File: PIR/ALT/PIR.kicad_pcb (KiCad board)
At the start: 2 copper layers, 30 x 90 mm, 29 parts, among them J1 BUS, J2 BATT_EXT, J5 FLASH/CONF, J6 PIR, Q1 BC846, Q2 BC846, Q3 BC857, SW1 tamper switch, U1 AP63203WU, U2 WT8266-S1

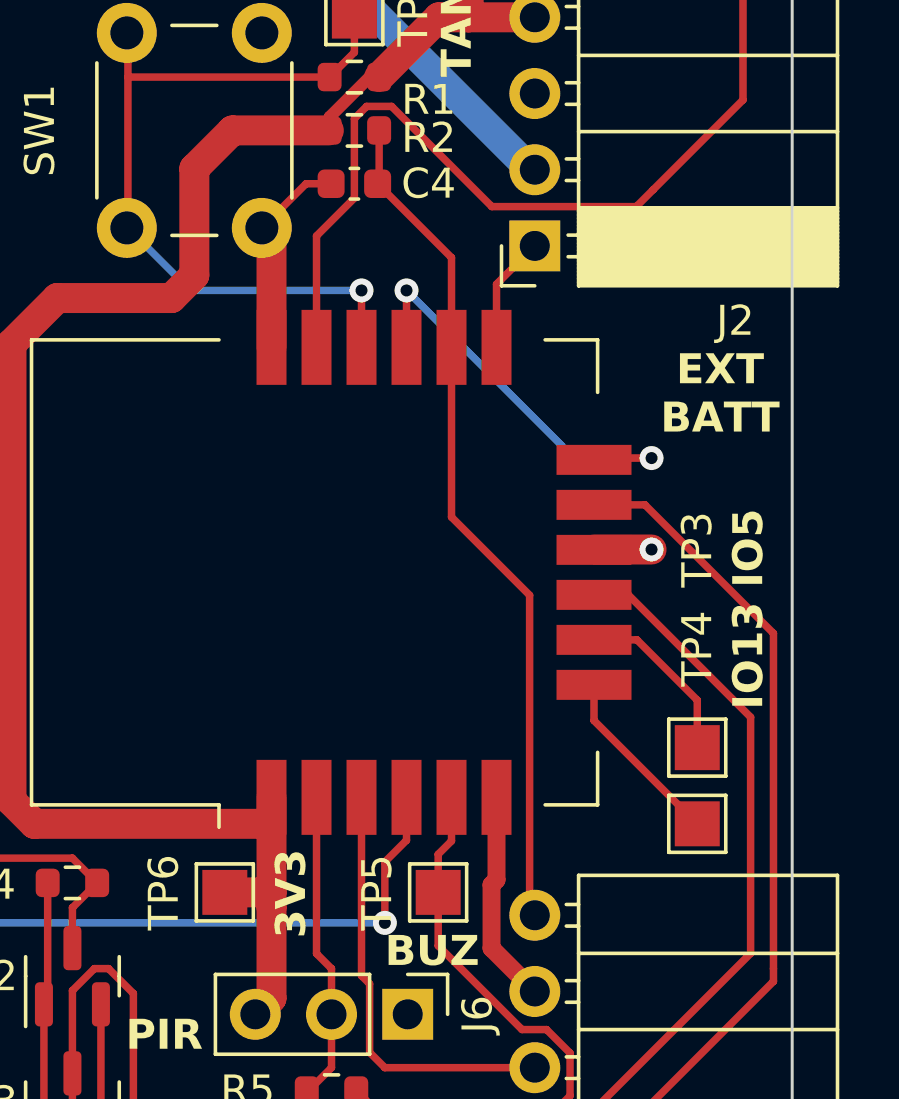
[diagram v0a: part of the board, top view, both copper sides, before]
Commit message: Update symbol and footprint of WT8266
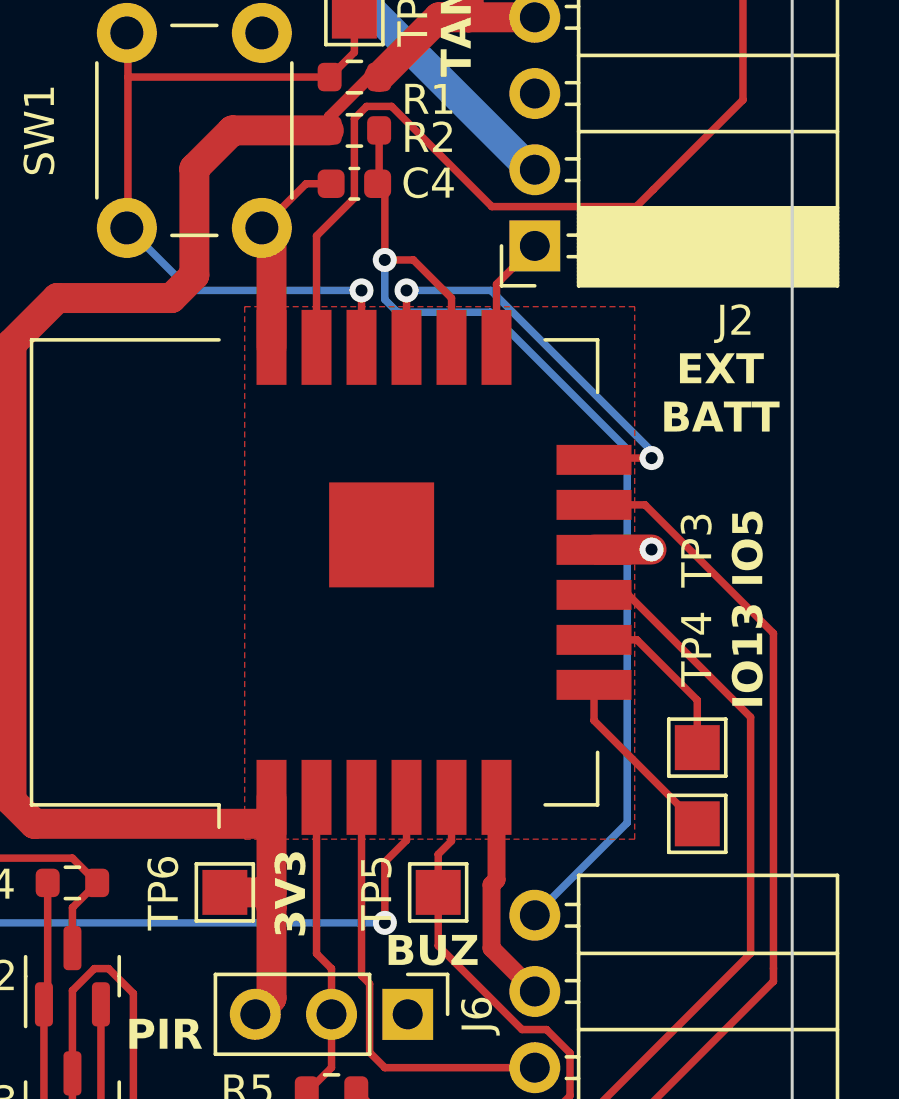
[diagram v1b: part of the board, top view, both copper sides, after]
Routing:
- net RST: track 28.0 -> 36.8 mm, vias 0 -> 1
- added copper zone on F.Cu, net GND

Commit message: Fix incident
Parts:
- added R6: 10k, Resistor_SMD:R_0603_1608Metric, F.Cu at (72.6, 130.0)
- turned C2 to 0 degrees
- renumbered J6 to J3, J5 to J4, R6 to R7, TP6 to TP2
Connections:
- C2 pad 1: Net-(U1-SW) -> Net-(U1-BST)
- C2 pad 2: Net-(U1-BST) -> Net-(U1-SW)
- L1 pad 1: Net-(U1-BST) -> Net-(U1-SW)
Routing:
- net Net-(U1-SW): track 2.14 -> 7.92 mm
- net Net-(U1-BST): track 7.63 -> 2.01 mm
- net I2C_D: track 79.7 -> 77.6 mm
- net +3.3V: track 75.8 -> 77.0 mm
- net GND: vias 2 -> 3
